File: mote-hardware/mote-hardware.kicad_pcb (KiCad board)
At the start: 2 copper layers, 93.6 x 102.8 mm, 60 parts, among them J1 USB_C_Receptacle_USB2.0_14P, J2 JST_XH2.54-SP, J4 SM03B-SRSS-TB, J6 Conn_01x03_Pin, J7 left_motor, J8 right_motor, SW1 SW_Push, SW2 SW_Push, U1 RP2354_60QFN, U2 NCP1117-3.3_SOT223, U4 RP Radio Module 2, U5 DRV8833PW, U9 LSM6DS3, Y1 ABM8-272-T3

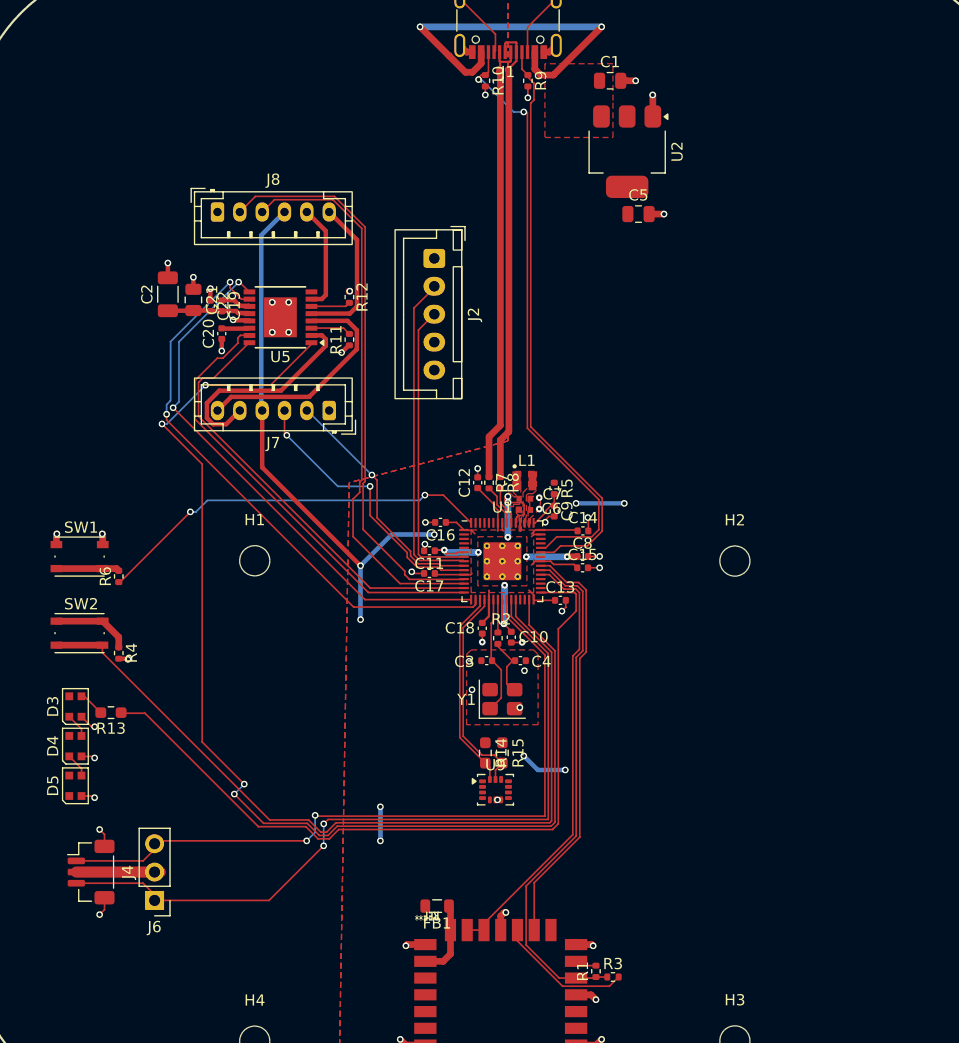
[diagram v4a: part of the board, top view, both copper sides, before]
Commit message: Selecting LCSC components
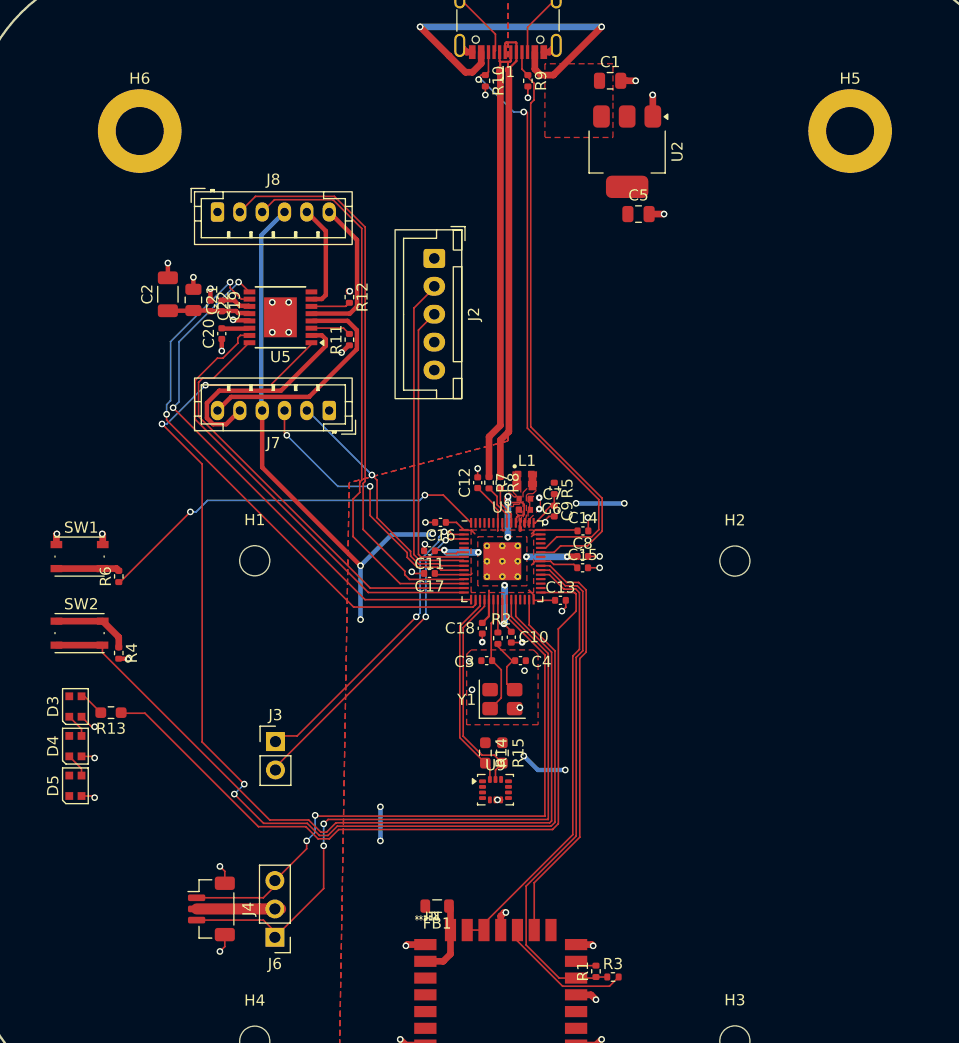
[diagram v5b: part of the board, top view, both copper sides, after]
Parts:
- added H5: MountingHole_Pad, MountingHole:MountingHole_4.3mm_M4_DIN965_Pad, F.Cu at (131.2, 54.5)
- added H6: MountingHole_Pad, MountingHole:MountingHole_4.3mm_M4_DIN965_Pad, F.Cu at (67.6, 54.5)
- added J3: Conn_01x02_Pin, Connector_PinHeader_2.54mm:PinHeader_1x02_P2.54mm_Vertical, F.Cu at (79.8, 109.2)
- moved J6 11.3 mm to (79.7, 126.7)
- moved J4 11.3 mm to (74.0, 124.2)
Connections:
- U1 pad 2: /rp2354/GPIO0 -> /rp2354/UART0_TX
- U1 pad 3: /rp2354/GPIO1 -> /rp2354/UART0_RX
- U5 pad 17: GND -> (no net)
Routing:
- net /rp2354/UART0_RX: track 0.00 -> 28.6 mm, vias 0 -> 2
- net /rp2354/UART0_TX: track 0.00 -> 27.8 mm, vias 0 -> 2
- net /rp2354/SWCLK: track 65.9 -> 56.9 mm
- net /rp2354/SWD: track 68.6 -> 61.5 mm

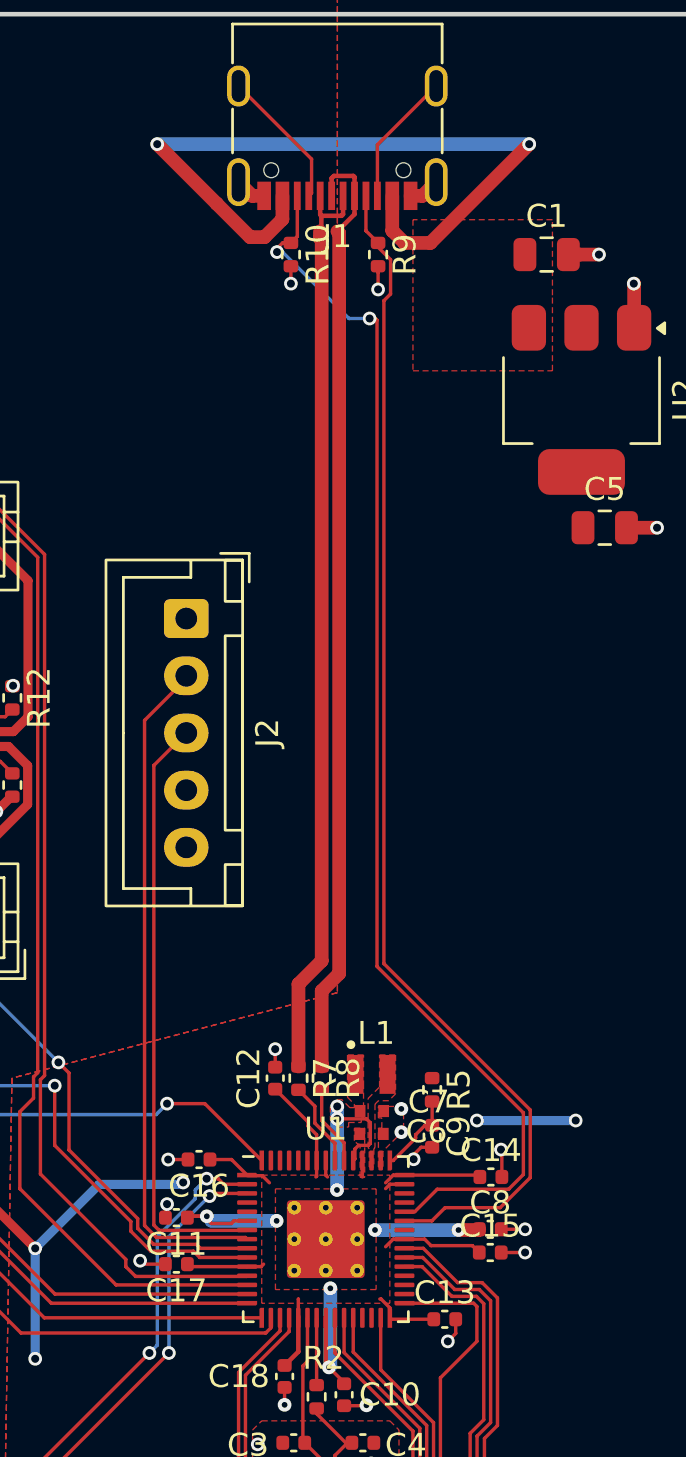
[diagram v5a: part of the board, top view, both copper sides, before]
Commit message: added led and did checks
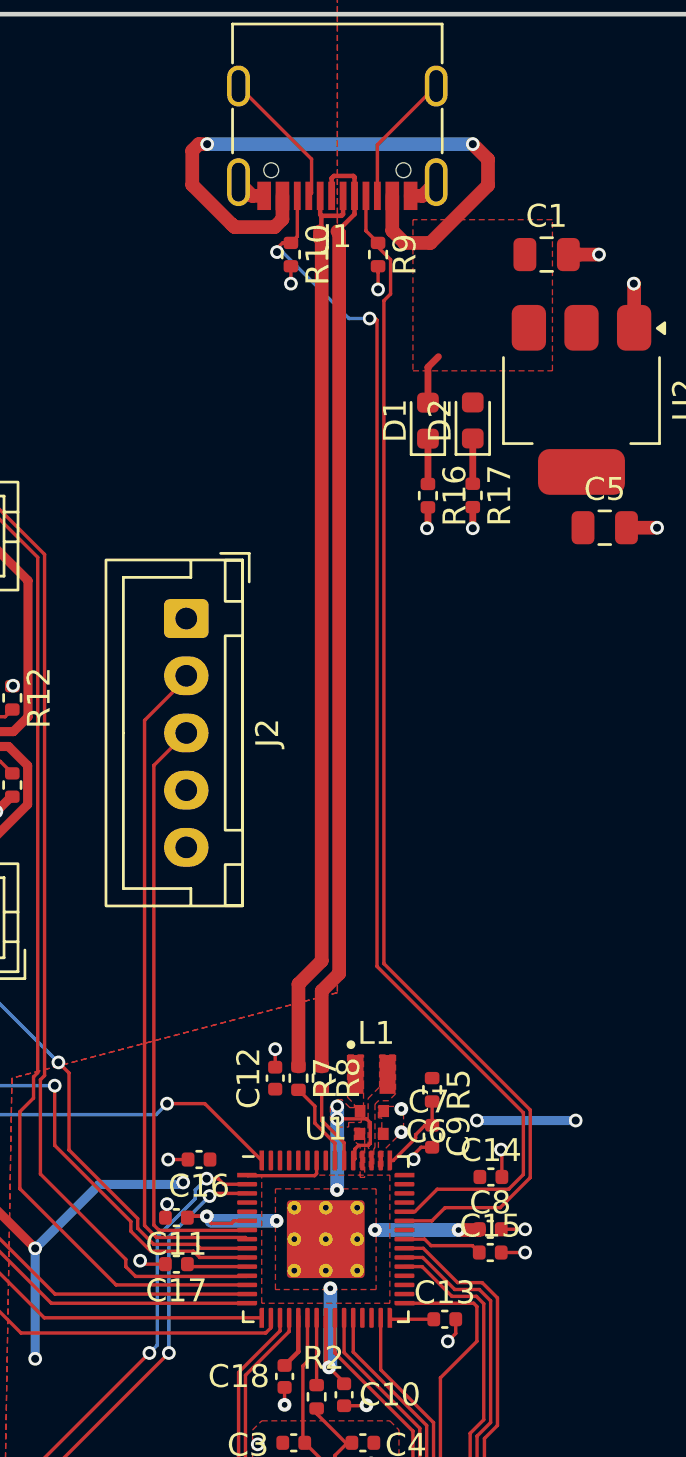
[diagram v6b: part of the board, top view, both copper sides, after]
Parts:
- added D1: LED, LED_SMD:LED_0603_1608Metric, F.Cu at (104.5, 57.3)
- added D2: LED, LED_SMD:LED_0603_1608Metric, F.Cu at (106.5, 57.3)
- added R16: 2.2k, Resistor_SMD:R_0402_1005Metric, F.Cu at (104.5, 60.6)
- added R17: 2.2k, Resistor_SMD:R_0402_1005Metric, F.Cu at (106.5, 60.6)
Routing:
- net /+3v3: track 85.3 -> 71.4 mm
- net /+5v: track 41.6 -> 38.3 mm
- net Net-(D2-K): track 0.00 -> 1.98 mm
- net Net-(D1-K): track 0.00 -> 1.98 mm
- net GND: track 69.5 -> 71.3 mm, vias 48 -> 50

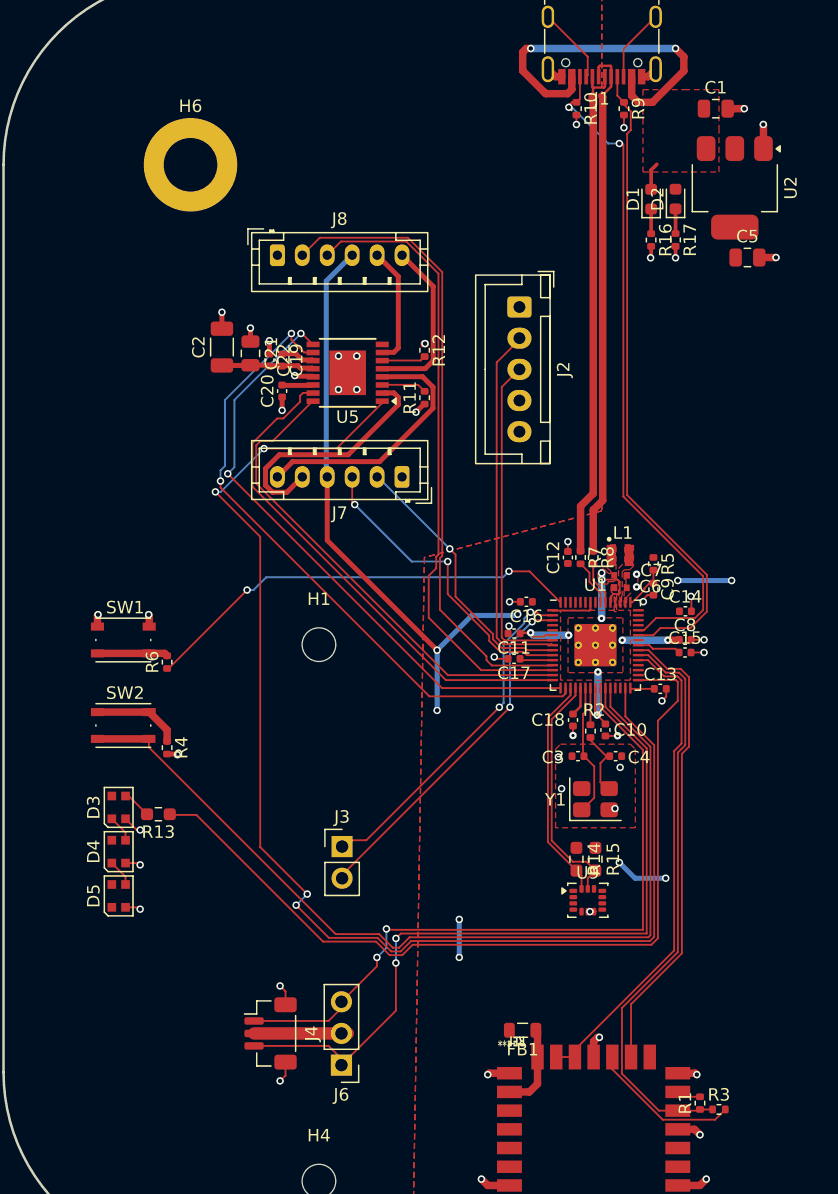
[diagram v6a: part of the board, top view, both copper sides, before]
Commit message: Finish selecting LCSC components
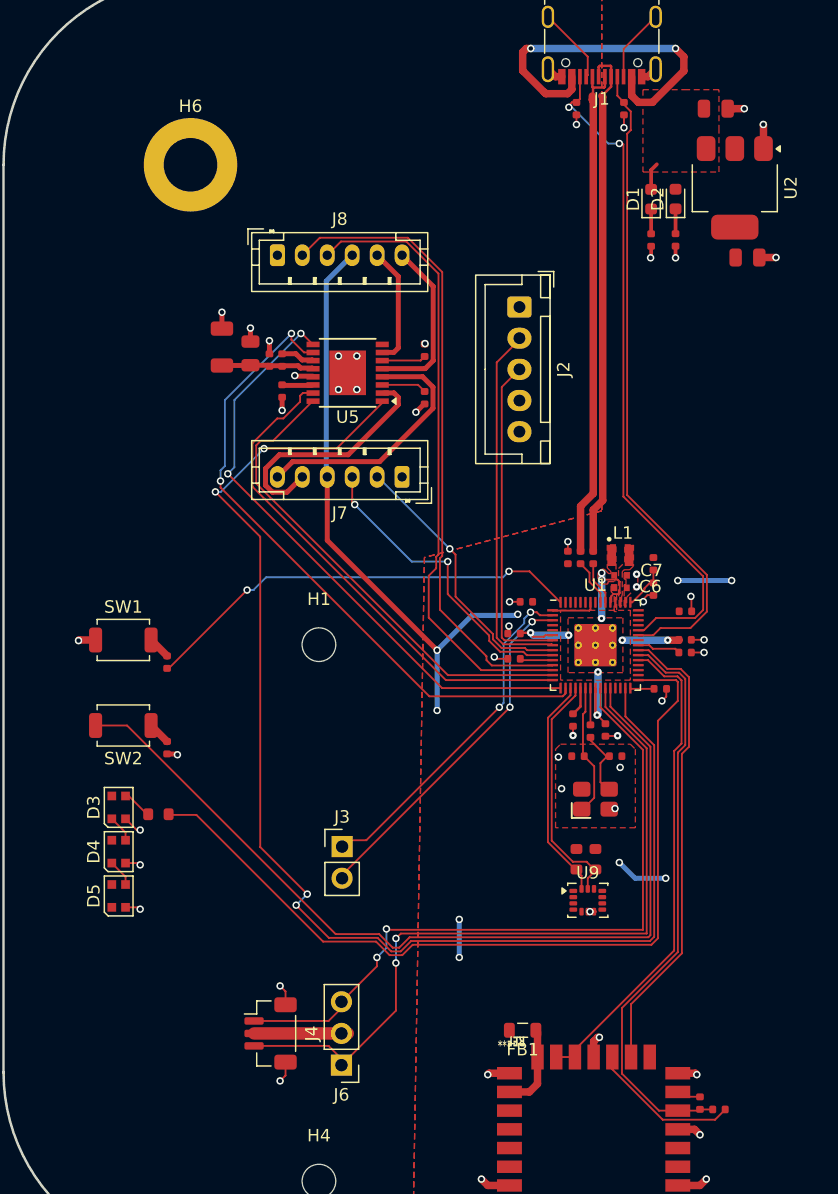
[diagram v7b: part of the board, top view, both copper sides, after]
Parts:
- C1, C21, C5: footprint Capacitor_SMD:C_0805_2012Metric -> PCM_JLCPCB:C_0805
- C10, C11, C12, C13, C14, C15, C16, C17, C18, C19, C20, C22, C3, C4, C8, C9: footprint Capacitor_SMD:C_0402_1005Metric -> PCM_JLCPCB:C_0402
- C2: footprint Capacitor_SMD:C_1206_3216Metric -> PCM_JLCPCB:C_1206
- R1, R10, R11, R12, R16, R17, R2, R3, R4, R5, R6, R7, R8, R9: footprint Resistor_SMD:R_0402_1005Metric -> PCM_JLCPCB:R_0402
- R13, R14, R15: footprint Resistor_SMD:R_0603_1608Metric_Pad0.98x0.95mm_HandSolder -> PCM_JLCPCB:R_0603
- SW1, SW2: footprint Button_Switch_SMD:SW_Push_1P1T_NO_Vertical_Wuerth_434133025816 -> Button_Switch_SMD:SW_SPST_TS-1088-xR020
- Y1: footprint Crystal:Crystal_SMD_3225-4Pin_3.2x2.5mm -> PCM_JLCPCB:CRYSTAL-SMD_4P-L3.2-W2.5-BL
- turned SW2 to 180 degrees
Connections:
- D2 pad 2: /+3v3 -> /status leds/+3v3
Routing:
- net Net-(R4-Pad1): track 7.09 -> 1.81 mm
- net /rp2354/~{USB_BOOT}: track 5.66 -> 1.82 mm
- net GND: track 71.3 -> 70.8 mm, vias 50 -> 49

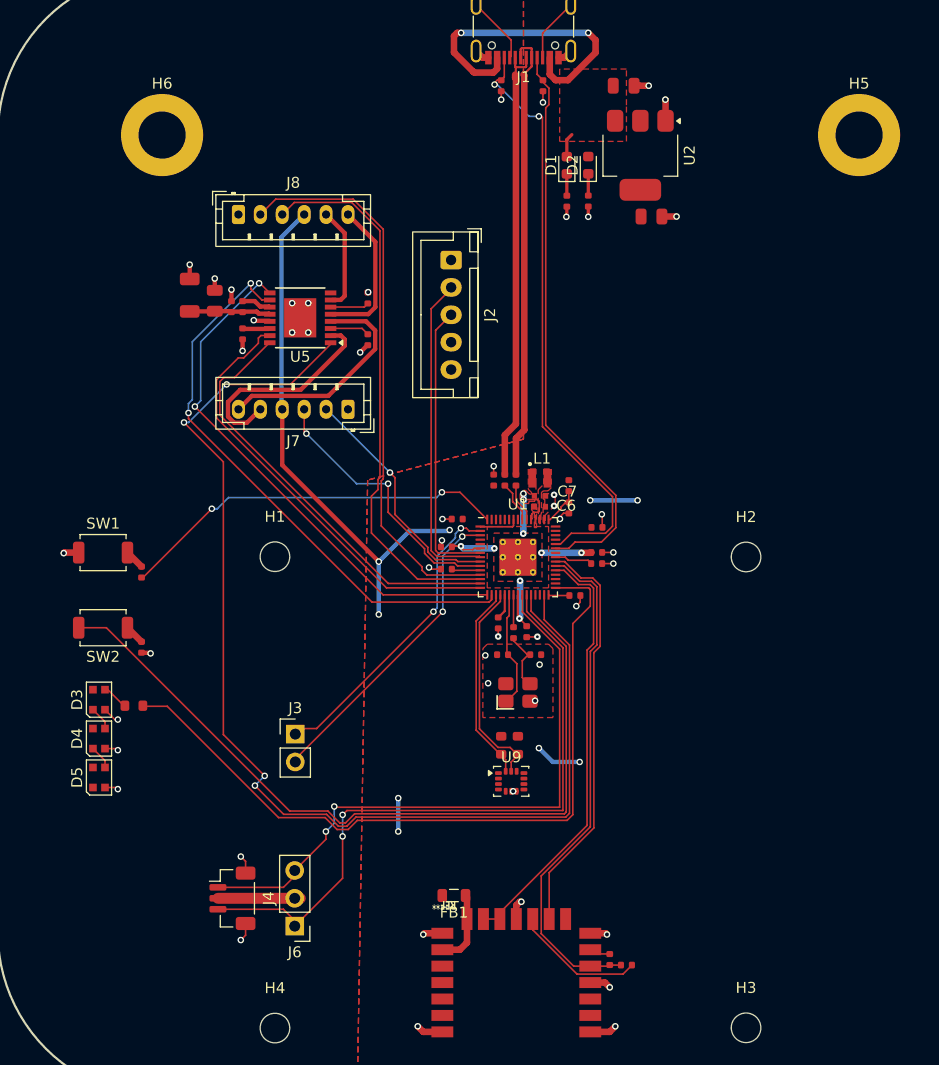
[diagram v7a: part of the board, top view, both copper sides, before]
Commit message: Fix DRC violations
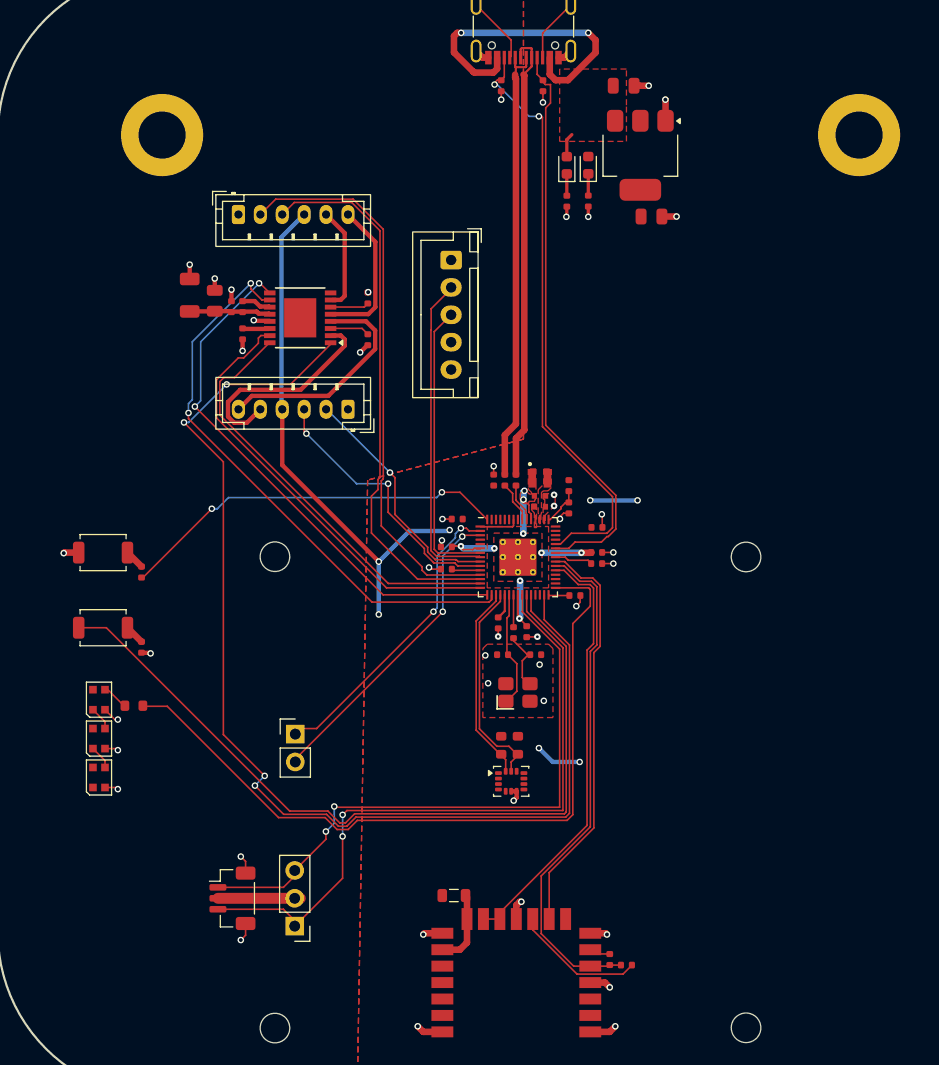
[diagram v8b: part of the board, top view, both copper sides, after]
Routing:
- net (no net): track 3.05 -> 0.00 mm, vias 2 -> 0
- net /rp2354/+1v1: track 25.0 -> 26.0 mm
- net /rp2354/UART0_TX: track 27.8 -> 27.0 mm
- net /rp2354/UART0_RX: track 28.6 -> 28.0 mm
- net GND: track 70.8 -> 71.4 mm, vias 49 -> 45
